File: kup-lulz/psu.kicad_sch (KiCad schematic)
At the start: 105 parts, among them J1 CONN_PCIE_PWR_8PIN, J2 CONN_IBC_MGMT, J3 CONN_01X03, J4 CONN_01X05, Q1 SSM6N58NU, SW1 SWITCH, SW2 SWITCH, U1 STM32L031C6U6, U2 MYMGK1R812ERSR, U3 MYMGK1R812ERSR, U4 MYMGK00506ERSR, U5 MYMGK00504ERSR, U7 MYMGK00504ERSR, U8 ADP1740ACPZ-1.8-R7

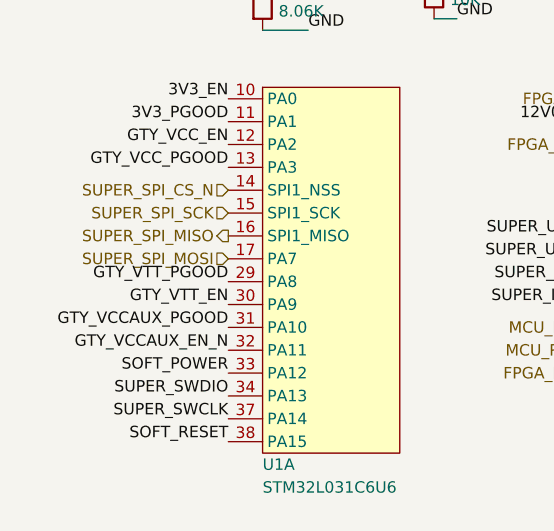
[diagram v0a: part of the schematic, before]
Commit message: Finished resolving all first-pass DRC errors (but not warnings)
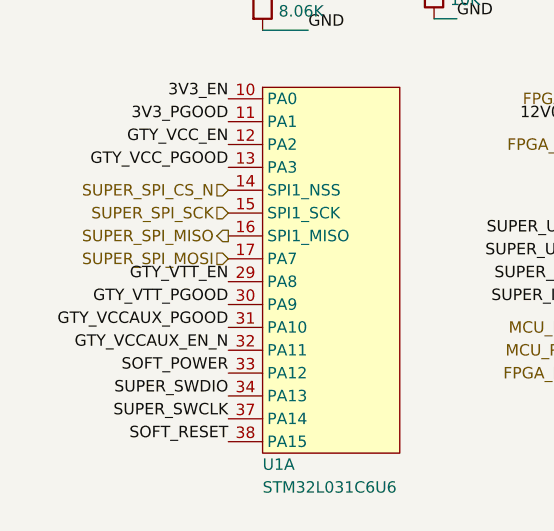
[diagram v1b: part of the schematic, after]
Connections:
- net GTY_VTT_EN: now also U1.29 (PA8); no longer U1.30 (PA9)
- net GTY_VTT_PGOOD: now also U1.30 (PA9); no longer U1.29 (PA8)
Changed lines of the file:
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@@
     (effects (font (size 1.27 1.27)) (justify left bottom))
   )
-  (label "GTY_VTT_PGOOD" (at 48.26 383.54 180)
+  (label "GTY_VTT_PGOOD" (at 48.26 386.08 180)
     (effects (font (size 1.27 1.27)) (justify right bottom))
   )
@@
     (effects (font (size 1.27 1.27)) (justify right bottom))
   )
-  (label "GTY_VTT_EN" (at 48.26 386.08 180)
+  (label "GTY_VTT_EN" (at 48.26 383.54 180)
     (effects (font (size 1.27 1.27)) (justify right bottom))
   )

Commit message: Fully routed and DRC clean, added stitching vias on 5mm grid. Still needs layer-change vias for diffpairs and connector launch optimization
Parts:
- added C14: 10 uF 25V, azonenberg_pcb:EIA_1210_CAP_NOSILK, symbol device:C
- added D3, D4: SZESD7471N2T5G, azonenberg_pcb:SOD882, symbol device:D_TVS
- added J13: FAN_01, azonenberg_pcb:CONN_MOLEX_KK_0470531000, symbol conn:CONN_01X04
- added R18: 10K, azonenberg_pcb:EIA_0402_RES_NOSILK, symbol device:R
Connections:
- net 12V0: now also C14.1, J13.2 (P2)
- net 3V3_SB: now also R18.2
- net GND: now also C14.2, D3.1 (A1), D4.1 (A1), J13.1 (P1)
- net FAN1_TACH: now reaches U1.39 (PB3)
- net FAN1_TACH: now also D3.2 (A2), J13.3 (P3), R18.1
- net FAN1_PWM: now reaches U1.40 (PB4)
- net FAN1_PWM: now also D4.2 (A2), J13.4 (P4)
- no-connect marks 6 -> 4
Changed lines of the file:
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@@
   (junction (at 67.31 184.15) (diameter 0) (color 0 0 0 0)
   )
+  (junction (at 387.35 260.35) (diameter 0) (color 0 0 0 0)
+  )
   (junction (at 67.31 168.91) (diameter 0) (color 0 0 0 0)
   )
@@
   (no_connect (at 91.44 396.24))
   (no_connect (at 91.44 401.32))
-  (no_connect (at 91.44 370.84))
-  (no_connect (at 91.44 373.38))
   (wire (pts (xy 67.31 214.63) (xy 67.31 217.17))
     (stroke (width 0) (type default) (color 0 0 0 0))
@@
     (stroke (width 0) (type default) (color 0 0 0 0))
   )
+  (wire (pts (xy 393.7 266.7) (xy 400.05 266.7))
+    (stroke (width 0) (type default) (color 0 0 0 0))
+  )
   (wire (pts (xy 398.78 152.4) (xy 398.78 154.94))
     (stroke (width 0) (type default) (color 0 0 0 0))
@@
     (stroke (width 0) (type default) (color 0 0 0 0))
   )
+  (wire (pts (xy 387.35 260.35) (xy 410.21 260.35))
+    (stroke (width 0) (type default) (color 0 0 0 0))
+  )
   (wire (pts (xy 265.43 111.76) (xy 280.67 111.76))
     (stroke (width 0) (type default) (color 0 0 0 0))
@@
     (stroke (width 0) (type default) (color 0 0 0 0))
   )
+  (wire (pts (xy 379.73 260.35) (xy 387.35 260.35))
+    (stroke (width 0) (type default) (color 0 0 0 0))
+  )
   (wire (pts (xy 222.25 171.45) (xy 222.25 173.99))
     (stroke (width 0) (type default) (color 0 0 0 0))
@@
     (effects (font (size 1.27 1.27)) (justify left bottom))
   )
+  (label "GND" (at 406.4 243.84 180)
+    (effects (font (size 1.27 1.27)) (justify right bottom))
+  )
   (label "GND" (at 88.9 30.48 180)
     (effects (font (size 1.27 1.27)) (justify right bottom))
@@
     (effects (font (size 1.27 1.27)) (justify right bottom))
   )
+  (label "3V3_SB" (at 400.05 266.7 0)
+    (effects (font (size 1.27 1.27)) (justify left bottom))
+  )
   (label "GTY_VTT_SENSE" (at 95.25 179.07 0)
     (effects (font (size 1.27 1.27)) (justify left bottom))
@@
     (effects (font (size 1.27 1.27)) (justify right bottom))
   )
+  (label "12V0" (at 406.4 236.22 180)
+    (effects (font (size 1.27 1.27)) (justify right bottom))
+  )
   (label "3V3_SB" (at 334.01 372.11 180)
     (effects (font (size 1.27 1.27)) (justify right bottom))
   )
+  (label "GND" (at 383.54 237.49 180)
+    (effects (font (size 1.27 1.27)) (justify right bottom))
+  )
   (label "SUPER_UART_RX" (at 91.44 381 180)
     (effects (font (size 1.27 1.27)) (justify right bottom))
@@
     (effects (font (size 1.27 1.27)) (justify right bottom))
   )
+  (label "FAN1_TACH" (at 386.08 266.7 180)
+    (effects (font (size 1.27 1.27)) (justify right bottom))
+  )
   (label "GND" (at 30.48 168.91 180)
     (effects (font (size 1.27 1.27)) (justify right bottom))
@@
     (effects (font (size 1.27 1.27)) (justify right bottom))
   )
+  (label "12V0" (at 383.54 240.03 180)
+    (effects (font (size 1.27 1.27)) (justify right bottom))
+  )
   (label "SUPER_SPI_MOSI" (at 322.58 405.13 180)
     (effects (font (size 1.27 1.27)) (justify right bottom))
@@
     (effects (font (size 1.27 1.27)) (justify right bottom))
   )
+  (label "FAN1_TACH" (at 387.35 252.73 180)
+    (effects (font (size 1.27 1.27)) (justify right bottom))
+  )
   (label "SUPER_LED1" (at 204.47 351.79 180)
     (effects (font (size 1.27 1.27)) (justify right bottom))
@@
     (effects (font (size 1.27 1.27)) (justify right bottom))
   )
+  (label "FAN1_PWM" (at 410.21 252.73 180)
+    (effects (font (size 1.27 1.27)) (justify right bottom))
+  )
   (label "GTY_VTT_EN" (at 67.31 234.95 180)
     (effects (font (size 1.27 1.27)) (justify right bottom))
@@
     (effects (font (size 1.27 1.27)) (justify right bottom))
   )
+  (label "FAN1_TACH" (at 383.54 242.57 180)
+    (effects (font (size 1.27 1.27)) (justify right bottom))
+  )
   (label "GND" (at 102.87 168.91 180)
     (effects (font (size 1.27 1.27)) (justify right bottom))
@@
     (effects (font (size 1.27 1.27)) (justify right bottom))
   )
+  (label "FAN1_TACH" (at 91.44 370.84 180)
+    (effects (font (size 1.27 1.27)) (justify right bottom))
+  )
   (label "3V3_SB" (at 73.66 337.82 0)
     (effects (font (size 1.27 1.27)) (justify left bottom))
@@
     (effects (font (size 1.27 1.27)) (justify left bottom))
   )
+  (label "FAN1_PWM" (at 91.44 373.38 180)
+    (effects (font (size 1.27 1.27)) (justify right bottom))
+  )
   (label "SUPER_LED0" (at 162.56 398.78 180)
     (effects (font (size 1.27 1.27)) (justify right bottom))
   )
+  (label "GND" (at 379.73 260.35 180)
+    (effects (font (size 1.27 1.27)) (justify right bottom))
+  )
   (label "SUPER_SPI_CS_N" (at 130.81 363.22 0)
     (effects (font (size 1.27 1.27)) (justify left bottom))
@@
     (effects (font (size 1.27 1.27)) (justify right bottom))
   )
+  (label "FAN1_PWM" (at 383.54 245.11 180)
+    (effects (font (size 1.27 1.27)) (justify right bottom))
+  )
   (label "1V8_PGOOD" (at 245.11 176.53 0)
     (effects (font (size 1.27 1.27)) (justify left bottom))
@@
     (pin "27")
     (pin "28")
-    (pin "39")
-    (pin "40")
+    (pin "39" (alternate "TIM2_CH2"))
+    (pin "40" (alternate "TIM22_CH1"))
     (pin "41")
     (pin "42" (alternate "USART2_TX"))
@@
     (pin "2")
   )
+  (symbol (lib_id "device:C") (at 406.4 240.03 0) (unit 1)
+    (in_bom yes) (on_board yes) (fields_autoplaced)
+    (property "Reference" "C14" (id 0) (at 409.321 239.1953 0)
+      (effects (font (size 1.27 1.27)) (justify left))
+    )
+    (property "Value" "10 uF 25V" (id 1) (at 409.321 241.7322 0)
+      (effects (font (size 1.27 1.27)) (justify left))
+    )
+    (property "Footprint" "azonenberg_pcb:EIA_1210_CAP_NOSILK" (id 2) (at 407.3652 243.84 0)
+      (effects (font (size 1.27 1.27)) hide)
+    )
+    (property "Datasheet" "" (id 3) (at 406.4 240.03 0)
+      (effects (font (size 1.27 1.27)) hide)
+    )
+    (pin "1")
+    (pin "2")
+  )
   (symbol (lib_id "device:R") (at 400.05 381 0) (unit 1)
     (in_bom yes) (on_board yes) (fields_autoplaced)
@@
     (pin "27")
     (pin "28")
-    (pin "39")
-    (pin "40")
+    (pin "39" (alternate "TIM2_CH2"))
+    (pin "40" (alternate "TIM22_CH1"))
     (pin "41")
     (pin "42" (alternate "USART2_TX"))
@@
     (pin "9")
   )
+  (symbol (lib_id "device:R") (at 389.89 266.7 90) (unit 1)
+    (in_bom yes) (on_board yes)
+    (property "Reference" "R18" (id 0) (at 394.97 265.43 90))
+    (property "Value" "10K" (id 1) (at 389.89 266.7 90))
+    (property "Footprint" "azonenberg_pcb:EIA_0402_RES_NOSILK" (id 2) (at 389.89 268.478 90)
+      (effects (font (size 1.27 1.27)) hide)
+    )
+    (property "Datasheet" "" (id 3) (at 389.89 266.7 0)
+      (effects (font (size 1.27 1.27)) hide)
+    )
+    (pin "1")
+    (pin "2")
+  )
   (symbol (lib_id "conn:CONN_01X03") (at 294.64 400.05 0) (unit 1)
     (in_bom yes) (on_board yes)
@@
     (pin "27")
     (pin "28")
-    (pin "39")
-    (pin "40")
+    (pin "39" (alternate "TIM2_CH2"))
+    (pin "40" (alternate "TIM22_CH1"))
     (pin "41")
     (pin "42" (alternate "USART2_TX"))
@@
     (pin "27")
     (pin "28")
-    (pin "39")
-    (pin "40")
+    (pin "39" (alternate "TIM2_CH2"))
+    (pin "40" (alternate "TIM22_CH1"))
     (pin "41")
     (pin "42" (alternate "USART2_TX"))
@@
     (pin "6")
   )
+  (symbol (lib_id "conn:CONN_01X04") (at 388.62 241.3 0) (unit 1)
+    (in_bom yes) (on_board yes) (fields_autoplaced)
+    (property "Reference" "J13" (id 0) (at 390.525 240.4653 0)
+      (effects (font (size 1.27 1.27)) (justify left))
+    )
+    (property "Value" "FAN_01" (id 1) (at 390.525 243.0022 0)
+      (effects (font (size 1.27 1.27)) (justify left))
+    )
+    (property "Footprint" "azonenberg_pcb:CONN_MOLEX_KK_0470531000" (id 2) (at 388.62 241.3 0)
+      (effects (font (size 1.27 1.27)) hide)
+    )
+    (property "Datasheet" "" (id 3) (at 388.62 241.3 0)
+      (effects (font (size 1.27 1.27)) hide)
+    )
+    (pin "1")
+    (pin "2")
+    (pin "3")
+    (pin "4")
+  )
   (symbol (lib_id "device:R") (at 208.28 351.79 270) (unit 1)
     (in_bom yes) (on_board yes) (fields_autoplaced)
@@
     (pin "2")
   )
+  (symbol (lib_id "device:D_TVS") (at 387.35 256.54 90) (unit 1)
+    (in_bom yes) (on_board yes) (fields_autoplaced)
+    (property "Reference" "D3" (id 0) (at 389.3566 255.7053 90)
+      (effects (font (size 1.27 1.27)) (justify right))
+    )
+    (property "Value" "SZESD7471N2T5G" (id 1) (at 389.3566 258.2422 90)
+      (effects (font (size 1.27 1.27)) (justify right))
+    )
+    (property "Footprint" "azonenberg_pcb:SOD882" (id 2) (at 387.35 256.54 0)
+      (effects (font (size 1.27 1.27)) hide)
+    )
+    (property "Datasheet" "https://en.wikipedia.org/wiki/Transient-voltage-suppression_diode" (id 3) (at 387.35 256.54 0)
+      (effects (font (size 1.27 1.27)) hide)
+    )
+    (pin "1")
+    (pin "2")
+  )
   (symbol (lib_id "passive-azonenberg:FERRITE_SMALL2") (at 78.74 22.86 0) (unit 1)
     (in_bom yes) (on_board yes)
@@
     (pin "27")
     (pin "28")
-    (pin "39")
-    (pin "40")
+    (pin "39" (alternate "TIM2_CH2"))
+    (pin "40" (alternate "TIM22_CH1"))
     (pin "41")
     (pin "42" (alternate "USART2_TX"))
@@
       (effects (font (size 1.27 1.27)) hide)
     )
+    (pin "1")
+    (pin "2")
+  )
+  (symbol (lib_id "device:D_TVS") (at 410.21 256.54 90) (unit 1)
+    (in_bom yes) (on_board yes) (fields_autoplaced)
+    (property "Reference" "D4" (id 0) (at 412.2166 255.7053 90)
+      (effects (font (size 1.27 1.27)) (justify right))
+    )
+    (property "Value" "SZESD7471N2T5G" (id 1) (at 412.2166 258.2422 90)
+      (effects (font (size 1.27 1.27)) (justify right))
+    )
+    (property "Footprint" "azonenberg_pcb:SOD882" (id 2) (at 410.21 256.54 0)
+      (effects (font (size 1.27 1.27)) hide)
+    )
+    (property "Datasheet" "https://en.wikipedia.org/wiki/Transient-voltage-suppression_diode" (id 3) (at 410.21 256.54 0)
+      (effects (font (size 1.27 1.27)) hide)
+    )

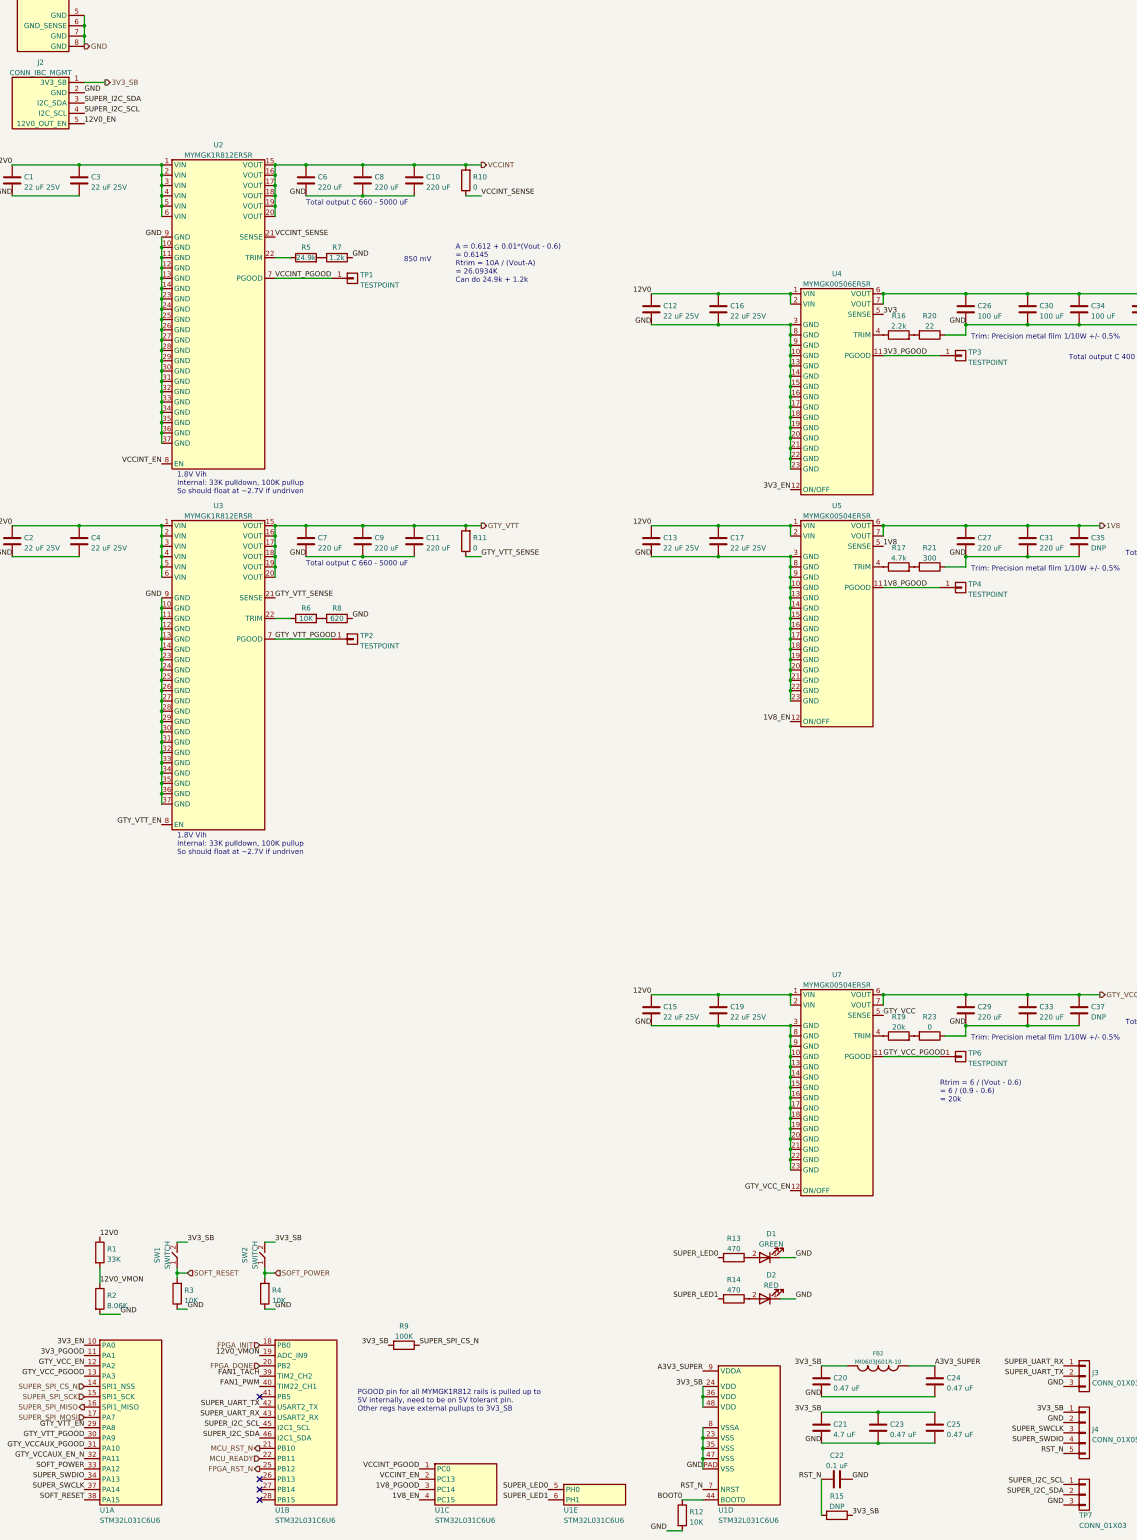
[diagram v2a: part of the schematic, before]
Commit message: Fixed ivnerted IBC management symbol
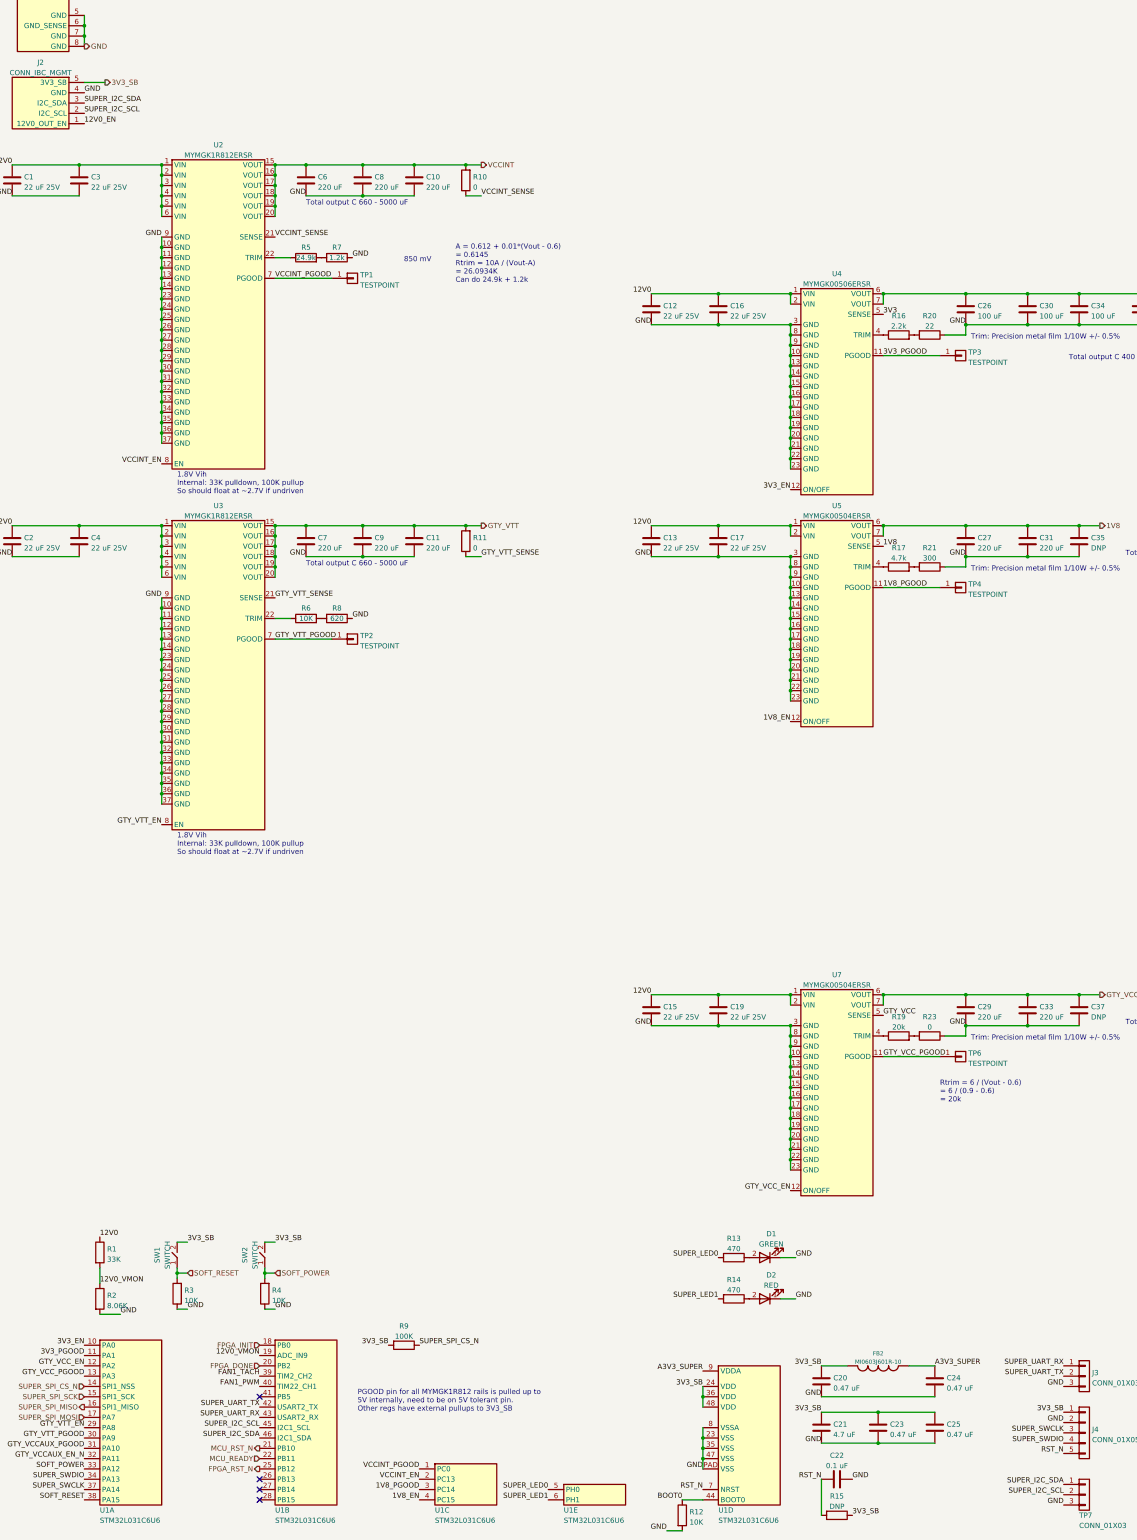
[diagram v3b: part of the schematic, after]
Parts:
- J2: symbol power-azonenberg:CONN_IBC_MGMT -> power-azonenberg:CONN_IBC_MGMT_DEVICE
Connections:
- net 12V0_EN: now also J2.1 (12V0_OUT_EN); no longer J2.5 (12V0_OUT_EN)
- net 3V3_SB: now also J2.5 (3V3_SB); no longer J2.1 (3V3_SB)
- net GND: now also J2.4 (GND); no longer J2.2 (GND)
- net SUPER_I2C_SCL: now also J2.2 (I2C_SCL), TP7.2 (P2); no longer J2.4 (I2C_SCL), TP7.1 (P1)
- net SUPER_I2C_SDA: now also TP7.1 (P1); no longer TP7.2 (P2)
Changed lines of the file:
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@@
   (title_block
     (title "Kintex Ultrascale+ OshPark For The Lulz")
-    (date "2024-02-22")
+    (date "2024-02-25")
     (rev "0.1")
     (company "Antikernel Labs")
@@
     (effects (font (size 1.27 1.27)) (justify right bottom))
   )
-  (label "SUPER_I2C_SCL" (at 289.56 397.51 180)
+  (label "SUPER_I2C_SCL" (at 289.56 400.05 180)
     (effects (font (size 1.27 1.27)) (justify right bottom))
   )
@@
     (effects (font (size 1.27 1.27)) (justify left bottom))
   )
-  (label "SUPER_I2C_SDA" (at 289.56 400.05 180)
+  (label "SUPER_I2C_SDA" (at 289.56 397.51 180)
     (effects (font (size 1.27 1.27)) (justify right bottom))
   )
@@
     (pin "2")
   )
-  (symbol (lib_id "power-azonenberg:CONN_IBC_MGMT") (at 44.45 63.5 0) (unit 1)
+  (symbol (lib_id "power-azonenberg:CONN_IBC_MGMT_DEVICE") (at 44.45 63.5 0) (unit 1)
     (in_bom yes) (on_board yes) (fields_autoplaced)
     (property "Reference" "J2" (id 0) (at 37.465 47.151 0))
